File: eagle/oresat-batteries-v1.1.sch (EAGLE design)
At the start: 69 parts, among them IC1 74AHC1G08DBV, U1 TCAN330, U2 STM32F042K6, U3 LTC4411, U4 LTC4411, U5 LTC4411, U6 LTC4411, U7 LTC4412, U8 LTC4412, X1 16MHz

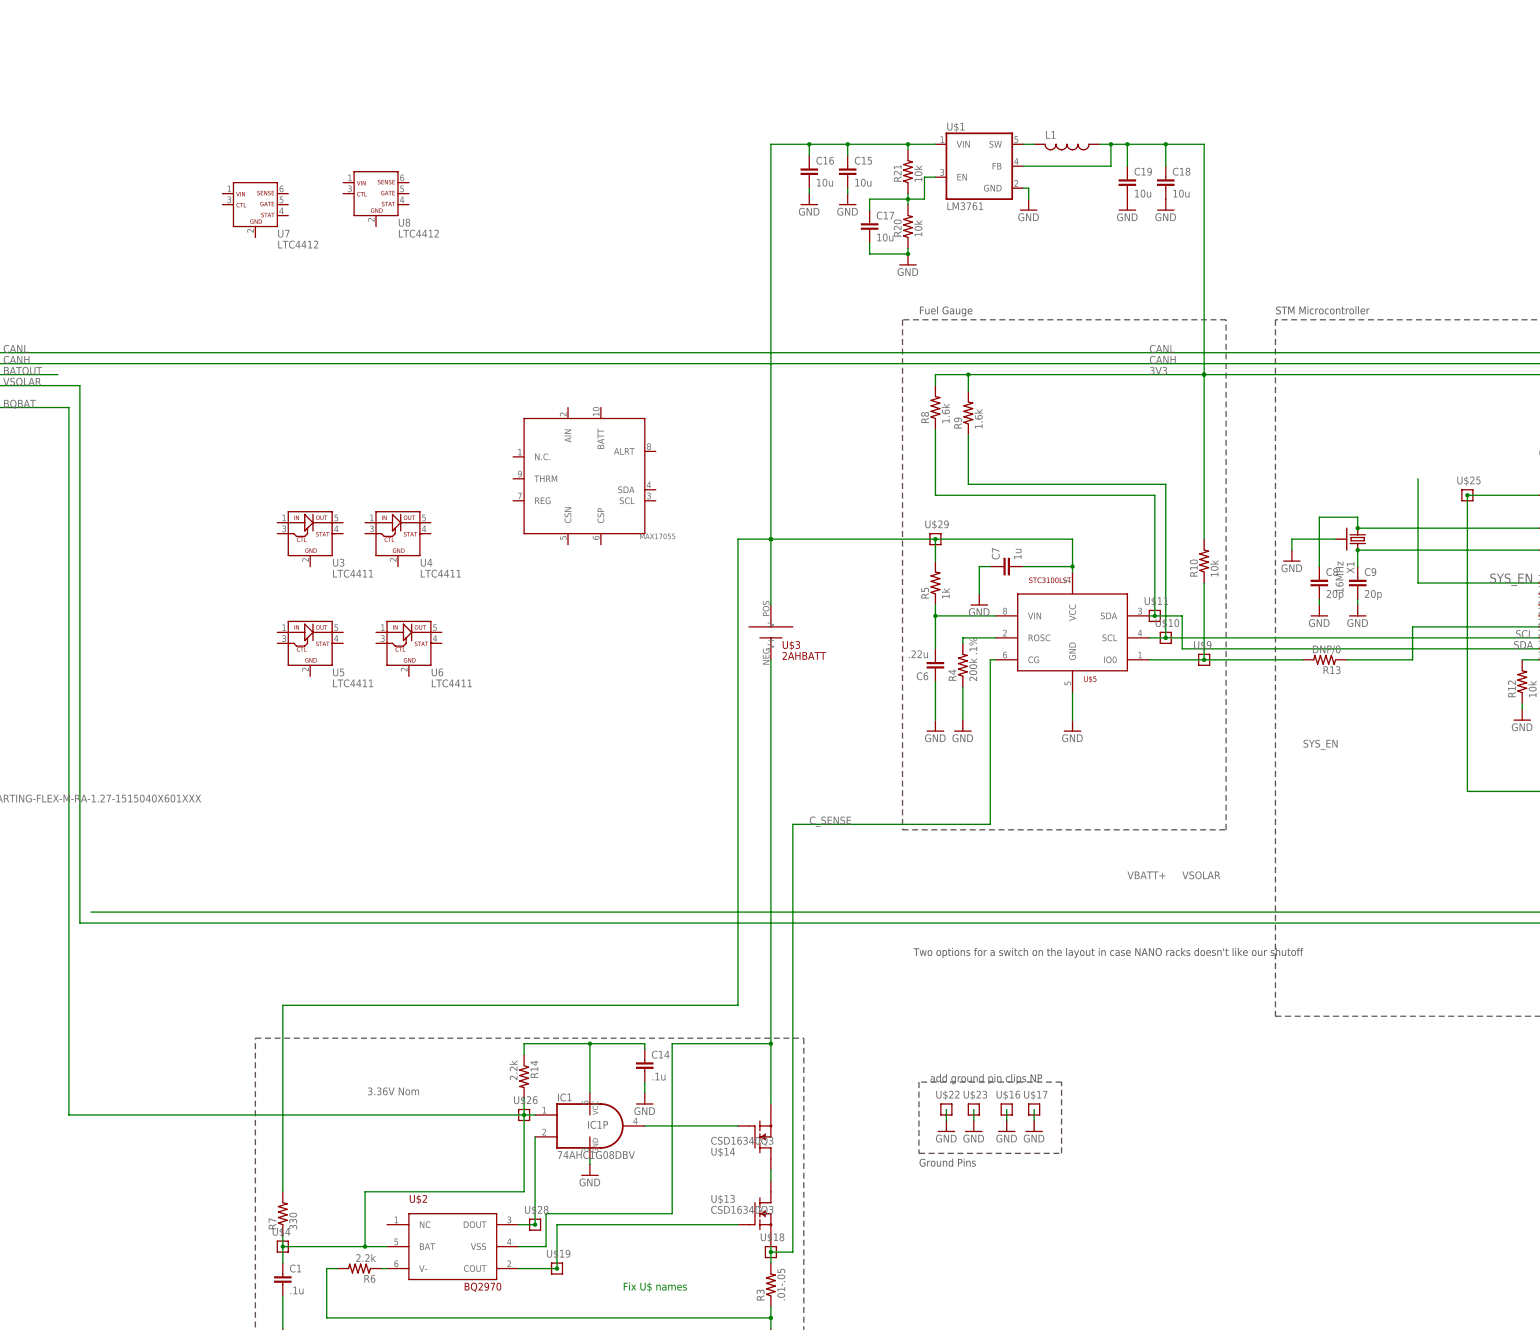
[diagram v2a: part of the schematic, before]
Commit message: Added 4412 and toshiba P-Channel Mosfets.
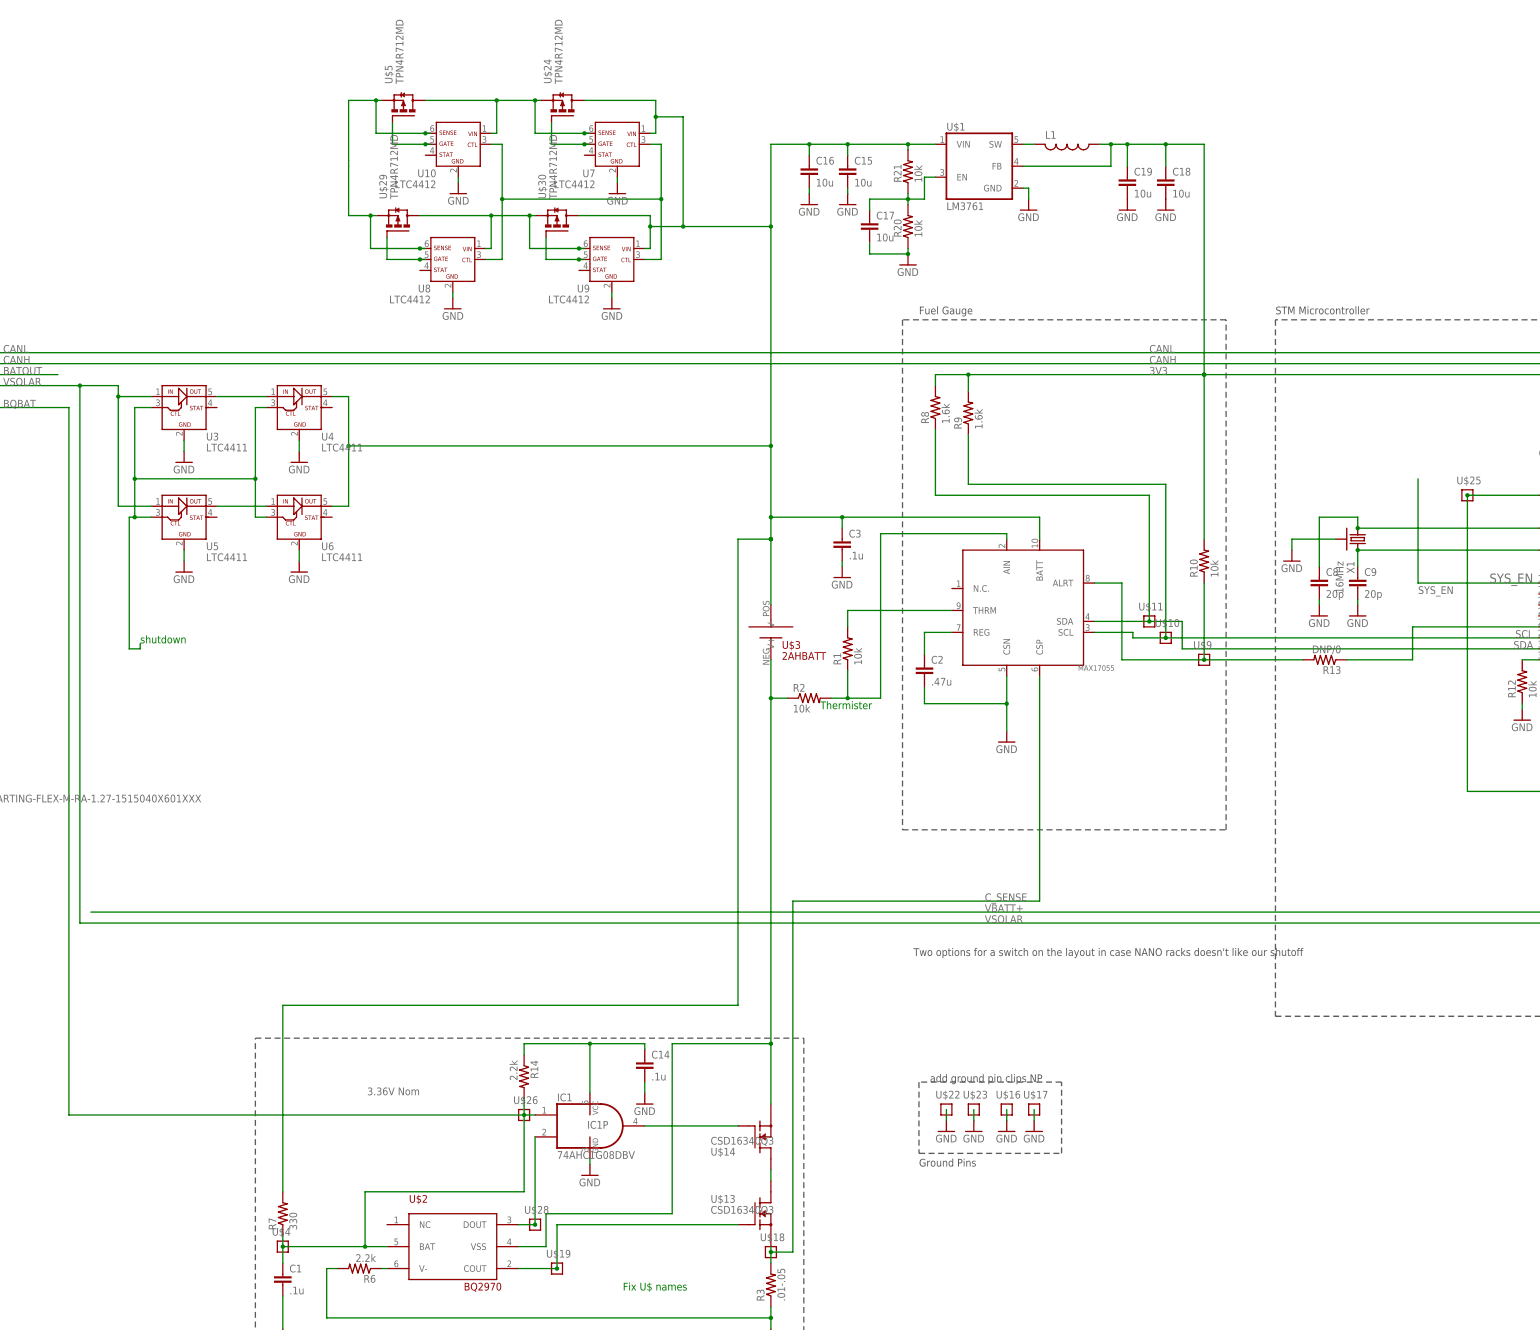
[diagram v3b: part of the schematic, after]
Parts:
- removed C6: .22u, rcl:C-EUC0603
- removed C7: 1u, rcl:C-EUC0805
- removed R4: 200k .1%, rcl:R-US_R0603
- removed R5: 1k, rcl:R-US_R0603
- added C2: .47u, rcl:C-EUC0603
- added C3: .1u, rcl:C-EUC0603
- added R1, R2: 10k, rcl:R-US_R0603
- added U$24, U$30: TPN4R712MD, tpn4r712md-pmosfet:TPN4R712MD
- added U10, U9: LTC4412, ltc4412:LTC4412
- U$29: value TP -> TPN4R712MD; device oresat-batteries:TP -> tpn4r712md-pmosfet:TPN4R712MD
- U$5: value STC3100LST -> TPN4R712MD; device oresat-batteries:STC3100LST -> tpn4r712md-pmosfet:TPN4R712MD
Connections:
- removed net IO0: R10.1, R13.2, U$5.IO0, U$9.P$1
- removed net ROSC: R4.2, U$5.ROSC
- removed net STC_CG: U$14.S, U$2.VSS, U$3.V-
- removed net STC_VIN: C6.2, R5.1, U$5.VIN
- new net 4411MB: U5.OUT, U6.IN
- new net 4411_MT: U3.OUT, U4.IN
- new net ALERT: R10.1, R13.2, U$6.ALRT, U$9.P$1
- new net BATT+: C15.1, C16.1, C3.1, R21.2, R7.2, U$1.VIN, U$24.D, U$3.V+, U$30.D, U$6.BATT, U4.OUT, U6.OUT, U7.VIN, U9.VIN
- new net BATT-: R2.1, U$14.S, U$2.VSS, U$3.V-
- new net CHG_SHD: U3.CTL, U4.CTL, U5.CTL, U6.CTL
- new net DSCHG_SHD: U10.CTL, U7.CTL, U8.CTL, U9.CTL
- new net N$11: U$24.S, U$5.D, U10.VIN, U7.SENSE
- new net N$12: U$24.G, U7.GATE
- new net N$16: U$29.G, U8.GATE
- new net N$18: U$29.D, U$30.S, U8.VIN, U9.SENSE
- new net N$19: U$30.G, U9.GATE
- new net N$8: U$5.G, U10.GATE
- new net REG: C2.1, U$6.REG
- new net THRM: R1.2, U$6.THRM
- new net VBATT: U$29.S, U$5.S, U10.SENSE, U8.SENSE
- net C_SENSE: now also U$6.CSP; no longer U$5.CG
- net GND: now also C2.2, C3.2, U$6.CSN, U10.GND, U3.GND, U4.GND, U5.GND, U6.GND, U7.GND, U8.GND, U9.GND; no longer C6.1, C7.1, R4.1, U$5.GND
- net N$3: now also R1.1, R2.2, U$6.AIN; no longer C15.1, C16.1, C7.2, R21.2, R5.2, R7.2, U$1.VIN, U$29.P$1, U$3.V+, U$5.VCC
- net SCL: now also U$6.SCL; no longer U$5.SCL
- net SDA: now also U$6.SDA; no longer U$5.SDA
- net VSOLAR: now also U3.IN, U5.IN
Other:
- note added: "Thermister"
- note added: "shutdown"
- moved on the sheet: U$11, U3, U4, U5, U6, U7, U8

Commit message: Added charge and discharge control, lowside shutdown, test points and finished rough v1.1 design.
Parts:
- added R11, R15, R16, R17, R18, R23, R4, R5: 470k, rcl:R-US_R0603
- added R19, R22: 10k, rcl:R-US_R0603
- added U$31: MC74HC1G04DFT1GOSCT, MC74HC1G04DFT1GOSCT:MC74HC1G04DFT1GOSCT
- added U$32, U$33, U$34, U$35, U$36, U$37, U$38, U$39, U$40, U$41, U$42, U$43, U$44, U$45, U$46, U$47, U$48, U$49, U$50: TP, oresat-batteries:TP
- U$27: value TP -> MC74HC1G04DFT1GOSCT; device oresat-batteries:TP -> MC74HC1G04DFT1GOSCT:MC74HC1G04DFT1GOSCT
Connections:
- removed net BATOUT: CF1.3
- removed net BQBAT: C1.1, CF1.6, IC1A.I0, R14.2, R7.1, U$2.BAT, U$26.P$1, U$4.P$1
- removed net PA8: U$27.P$1, U2.PA8
- removed net SYS_EN: U2.PB0
- removed net VBATT: U$29.S, U$5.S, U10.SENSE, U8.SENSE
- removed net VBATT+: CF2.2
- new net CHG_CTL: CF1.7, R22.1, U$27.INA
- new net DCHG_CTL: CF1.9, R19.1, U$31.INA
- new net LOWSHD: C1.1, CF1.11, IC1A.I0, R14.2, R7.1, U$2.BAT, U$26.P$1, U$4.P$1
- new net U10STAT: R5.2, U10.STAT, U2.PB3
- new net U3STAT: R23.2, U2.PA8, U3.STAT
- new net U4STAT: R17.2, U2.PA6, U4.STAT
- new net U5STAT: R18.2, U2.PA7, U5.STAT
- new net U6STAT: R16.2, U2.PA5, U6.STAT
- new net U7STAT: R15.2, U2.PA4, U7.STAT
- new net U8STAT: R4.2, U2.PB4, U8.STAT
- new net U9STAT: R11.2, U2.PB1, U9.STAT
- net 3V3: now also CF2.2, R11.1, R15.1, R16.1, R17.1, R18.1, R23.1, R4.1, R5.1, U$38.P$1, U$39.P$1
- net BATT+: now also R19.2, R22.2, U$27.VCC, U$31.VCC, U$50.P$1
- net CANH: now also U$42.P$1
- net CANL: now also U$43.P$1
- net CHG_SHD: now also U$27.OUT, U$47.P$1, U$48.P$1
- net DSCHG_SHD: now also U$31.OUT, U$46.P$1
- net GND: now also U$27.GND, U$31.GND
- net NRESET: now also U$37.P$1
- net SCL: now also R8.1; no longer R9.1
- net SDA: now also R9.1; no longer R8.1
- net STM_DEBUG: now also U$32.P$1
- net SWCLK: now also U$36.P$1
- net SWDIO: now also U$35.P$1
- net USART2_RX: now also U$33.P$1, U$41.P$1, U$44.P$1
- net USART2_TX: now also U$34.P$1, U$40.P$1
- net VSOLAR: now also CF1.3, CF1.5, CF1.6, DEBUG_DNP.10, DEBUG_DNP.9, U$29.S, U$45.P$1, U$49.P$1, U$5.S, U10.SENSE, U8.SENSE
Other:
- note added: "- Do we need an inverter per ctl on the 441x chips? - Do we need the status of the 441X chips and should we control CHG and DCHG with the MCU? - Do we care about MAX alert pin? - Still need to select a thermister. - Still need to select fuses. - Look at heater. - What do you think of these P-FETs? - Recalculate i2c pull-ups. - Change test points from U$ to TP*"
- note removed: "SYS_EN"
- note removed: "Two options for a switch on the layout in case NANO racks doesn't like our shutoff"
- note removed: "VBATT+"
- note removed: "add ground pin clips NP"
- note removed: "shutdown"
- moved on the sheet: C1, C10, C11, C12, C13, C14, C15, C16, C17, C18, C19, C2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

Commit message: Added double pin header.
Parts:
- removed R11, R15, R18, R23: 470k, rcl:R-US_R0603
- added JP2: (no value), pinhead:PINHD-2X20
- R8, R9: value 1.6k -> 4.7k
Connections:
- removed net LOWSHD: C1.1, CF1.11, IC1A.I0, R14.2, R7.1, U$2.BAT, U$26.P$1, U$4.P$1
- removed net N$6: C14.1, IC1P.VCC, R14.1
- removed net U10STAT: R5.2, U10.STAT, U2.PB3
- removed net U4STAT: R17.2, U2.PA6, U4.STAT
- removed net U5STAT: R18.2, U2.PA7, U5.STAT
- removed net U8STAT: R4.2, U2.PB4, U8.STAT
- new net N$4: U2.PA8
- new net SPARE1: CF1.19, CF1.20, JP2.19
- new net SPARE10: CF1.37, CF1.38, JP2.37
- new net SPARE11: CF1.39, CF1.40, JP2.39
- new net SPARE2: CF1.21, CF1.22, JP2.21
- new net SPARE3: CF1.23, CF1.24, JP2.23
- new net SPARE4: CF1.25, CF1.26, JP2.25
- new net SPARE5: CF1.27, CF1.28, JP2.27
- new net SPARE6: CF1.29, CF1.30, JP2.29
- new net SPARE7: CF1.31, CF1.32, JP2.31
- new net SPARE8: CF1.33, CF1.34, JP2.33
- new net SPARE9: CF1.35, CF1.36, JP2.35
- new net SYSSHD: C1.1, CF1.17, CF1.18, IC1A.I0, JP2.17, JP2.18, R14.2, R7.1, U$2.BAT, U$26.P$1, U$4.P$1
- net 3V3: no longer R11.1, R15.1, R18.1, R23.1
- net BATT+: now also C14.1, IC1P.VCC, R14.1
- net BATT-: no longer R2.1
- net CANH: now also CF1.3, CF1.4, JP2.3, JP2.4; no longer CF1.2
- net CANL: now also CF1.2, JP2.1, JP2.2
- net CHG_CTL: now also CF1.13, CF1.14, JP2.13, JP2.14; no longer CF1.7
- net C_SENSE: now also R2.1, R6.2
- net DCHG_CTL: now also CF1.15, CF1.16, JP2.15, JP2.16; no longer CF1.9
- net GND: now also CF1.11, CF1.12, CF1.5, CF1.6, JP2.11, JP2.5; no longer R6.2
- net U3STAT: now also R17.2, U2.PA6, U4.STAT; no longer R23.2, U2.PA8
- net U6STAT: now also U5.STAT
- net U7STAT: now also R5.2, U10.STAT, U2.PB3; no longer R15.2, U2.PA4
- net U9STAT: now also R4.2, U2.PB4, U8.STAT; no longer R11.2, U2.PB1
- net VSOLAR: now also CF1.10, CF1.7, CF1.8, CF1.9, JP2.6, JP2.7, JP2.8, JP2.9; no longer CF1.3, CF1.4, CF1.5, CF1.6
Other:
- moved on the sheet: CF1

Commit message: Fixed most of the issues from design review Sept 25.
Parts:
- removed C16, C17, C18, C19: 10u, rcl:C-EUC0805
- removed DEBUG_DNP: (no value), pinhead:PINHD-2X8
- removed R21, R22: 10k, rcl:R-US_R0603
- removed U$1: LM3761, oresat-batteries:LM3761
- removed U$13, U$14: CSD16340Q3, oresat-batteries:CSD16340Q3
- removed U$16, U$17, U$18, U$19, U$22, U$23, U$26, U$28, U$4, U$41, U$44, U$46, U$47, U$48, U$49, U$50: TP, oresat-batteries:TP
- removed U$2: BQ2970, oresat-batteries:BQ2970
- removed U$21: 4.19, oresat-batteries:RES_HEATER
- removed U$24, U$29, U$30, U$5: TPN4R712MD, tpn4r712md-pmosfet:TPN4R712MD
- removed U$27, U$31: MC74HC1G04DFT1GOSCT, MC74HC1G04DFT1GOSCT:MC74HC1G04DFT1GOSCT
- removed U$3: 2AHBATT, oresat-batteries:2AHBATT
- removed U$6: MAX17055, max17055:MAX17055
- added B1: 2AHBATT, oresat-batteries:2AHBATT
- added C4, C7: .1u, rcl:C-EUC0603
- added C5, C6: 10u, rcl:C-EUC0805
- added D1, D2, D3: CMDD6001, CMMDD6001:CMDD6001
- added JP1: (no value), pinhead:PINHD-2X20
- added Q1, Q2: CSD16340Q3, oresat-batteries:CSD16340Q3
- added Q3, Q4, Q5, Q6: TPN4R712MD, tpn4r712md-pmosfet:TPN4R712MD
- added R11: 4.7k, rcl:R-US_R0603
- added R15, R18: 470k, rcl:R-US_R0603
- added TP1, TP10, TP11, TP12, TP13, TP14, TP19, TP2, TP20, TP3, TP4, TP5, TP6, TP7, TP8, TP9: TP, oresat-batteries:TP
- added U11: MAX17055, max17055:MAX17055
- added U12, U13: LTC4412, ltc4412:LTC4412
- added U14: STM32F042K6, oresat-batteries:STM32F042K6
- added U15: TCAN330, oresat-batteries:TCAN330
- C1, C3: value .1u -> 10u; device rcl:C-EUC0603 -> rcl:C-EUC0805
- C10, C11: value 100n -> 20p
- C14: value .1u -> 100n
- C15: value 10u -> 100n; device rcl:C-EUC0805 -> rcl:C-EUC0603
- C2: value .47u -> 10u; device rcl:C-EUC0603 -> rcl:C-EUC0805
- C8: value 20p -> .1u
- C9: value 20p -> .47u
- JP2: device pinhead:PINHD-2X20 -> pinhead:PINHD-2X8
- R1: value 10k -> 330
- R12: value 10k -> 4.7k
- R13: value DNP/0 -> 10k
- R14: value 2.2k -> 470k
- R16: value 470k -> DNP/0
- R20: value 10k -> 4.19; device rcl:R-US_R0603 -> oresat-batteries:RES_HEATER
- R3: value .01-.05 -> 10k
- R4: value 470k -> 10k
- R5: value 470k -> 2.2k
- R7: value 330 -> .01-.05
- R8, R9: value 4.7k -> 10k
- U1: value TCAN330 -> LM3761; device oresat-batteries:TCAN330 -> oresat-batteries:LM3761
- U2: value STM32F042K6 -> MC74HC1G04DFT1GOSCT; device oresat-batteries:STM32F042K6 -> MC74HC1G04DFT1GOSCT:MC74HC1G04DFT1GOSCT
- U3: value LTC4411 -> BQ2970; device ltc4411:LTC4411 -> oresat-batteries:BQ2970
- U7: value LTC4412 -> LTC4411; device ltc4412:LTC4412 -> ltc4411:LTC4411
- U8: value LTC4412 -> MC74HC1G04DFT1GOSCT; device ltc4412:LTC4412 -> MC74HC1G04DFT1GOSCT:MC74HC1G04DFT1GOSCT
- renumbered CF1 to CM1, CF2 to J1, U$10 to TP15, U$11 to TP16, U$12 to TP31, U$15 to TP30, U$20 to Q7, U$25 to TP18, U$32 to TP23, U$33 to TP24, U$34 to TP25, U$35 to TP26, U$36 to TP27, U$37 to TP28, U$38 to TP29, U$39 to TP22, U$40 to TP21, U$42 to TP34, U$43 to TP33, U$45 to TP35, U$8 to TP32, U$9 to TP17
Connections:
- removed net 3V3: C10.1, C11.1, C12.1, C13.1, C18.1, C19.1, DEBUG_DNP.1, DEBUG_DNP.2, J1.2, L1.1, Q7.D, R10.2, R16.1, R17.1, R4.1, R5.1, R8.2, R9.2, TP22.P$1, TP29.P$1, TP30.P$1, U$1.FB, U1.VCC, U2.VDD, U2.VDDA, U2.VDDIO2
- removed net BATT+: C14.1, C15.1, C16.1, C3.1, IC1P.VCC, R14.1, R19.2, R21.2, R22.2, R7.2, U$1.VIN, U$24.D, U$27.VCC, U$3.V+, U$30.D, U$31.VCC, U$50.P$1, U$6.BATT, U4.OUT, U6.OUT, U7.VIN, U9.VIN
- new net 3.3V: C12.1, C13.1, C14.1, C15.1, C5.1, C6.1, J1.2, JP2.1, JP2.2, L1.1, Q7.D, R11.2, R12.2, R13.2, R14.1, R15.1, R17.1, R18.1, TP22.P$1, TP29.P$1, TP30.P$1, U1.FB, U14.VDD, U14.VDDA, U14.VDDIO2, U15.VCC
- new net N$10: D3.A, R4.1, U2.INA
- new net N$6: D1.C, JP1.18
- new net N$9: D2.C, JP1.16
- new net VBATT: B1.V+, C1.1, C2.1, C7.1, C8.1, IC1P.VCC, Q3.D, Q4.D, R1.2, R2.2, R4.2, R6.1, R8.2, TP12.P$1, U1.VIN, U10.VIN, U11.BATT, U2.VCC, U6.OUT, U7.OUT, U8.VCC, U9.VIN
- net 4411MB: now also U7.IN; no longer U6.IN
- net 4411_MT: now also U4.OUT, U6.IN; no longer U3.OUT, U4.IN
- net ALERT: now also R13.1, R16.2, U11.ALRT; no longer R10.1, R13.2, U$6.ALRT
- net ANDDRIVE: now also Q1.G; no longer U$14.G
- net BATT-: now also B1.V-, Q1.S, U3.VSS; no longer U$14.S, U$2.VSS, U$3.V-
- net BETSHUT: now also Q1.D, Q2.D; no longer U$13.D, U$14.D
- net BQVMIN: now also R5.1, U3.V-; no longer R6.1, U$2.V-
- net CANH: now also JP1.3, JP1.4, JP2.13, JP2.14, U15.CANH; no longer DEBUG_DNP.13, DEBUG_DNP.14, JP2.3, JP2.4, U1.CANH
- net CANL: now also JP1.1, JP1.2, JP2.11, JP2.12, U15.CANL; no longer DEBUG_DNP.11, DEBUG_DNP.12, JP2.1, JP2.2, U1.CANL
- net CAN_EN: now also U14.PA10, U15.SHDN; no longer U1.SHDN, U2.PA10
- net CAN_LSTN: now also U14.PA9, U15.S; no longer U1.S, U2.PA9
- net CAN_RX: now also U14.PA11, U15.RXD; no longer U1.RXD, U2.PA11
- net CAN_TX: now also U14.PA12, U15.TXD; no longer U1.TXD, U2.PA12
- net CHG_CTL: now also D3.C, JP1.13, JP1.14; no longer JP2.13, JP2.14, R22.1, U$27.INA
- net CHG_SHD: now also TP10.P$1, TP11.P$1, U2.OUT, U7.CTL; no longer U$27.OUT, U$47.P$1, U$48.P$1, U3.CTL
- net COUT: now also Q2.G, TP9.P$1, U3.COUT; no longer U$13.G, U$19.P$1, U$2.COUT
- net C_SENSE: now also Q2.S, R5.2, R7.2, R9.1, TP13.P$1, U11.CSP; no longer R2.1, R3.2, R6.2, U$13.S, U$18.P$1, U$6.CSP
- net DCHG_CTL: now also D2.A, JP1.15, R8.1, U8.INA; no longer JP2.15, JP2.16, R19.1, U$31.INA
- net DSCHG_SHD: now also TP14.P$1, U12.CTL, U13.CTL, U8.OUT; no longer U$31.OUT, U$46.P$1, U7.CTL, U8.CTL
- net GND: now also C4.2, C5.2, C6.2, C7.2, JP1.11, JP1.5, JP2.15, JP2.16, R19.1, R20.2, R7.1, TP1.P$1, TP2.P$1, TP3.P$1, TP4.P$1, U11.CSN, U12.GND, U13.GND, U14.VSS, U15.GND, U2.GND; no longer C16.2, C17.2, C18.2, C19.2, DEBUG_DNP.15, DEBUG_DNP.16, JP2.11, JP2.5, R12.1, R20.1, U$1.GND, U$16.P$1, U$17.P$1, U$21.2, U$22.P$1, U$23.P$1, U$27.GND, U$31.GND, U$6.CSN, U2.VSS, U3.GND
- net HEAT: now also U14.PA1; no longer U2.PA1
- net N$1: now also U1.SW; no longer U$1.SW
- net N$11: now also Q3.S, Q5.D, U12.VIN, U9.SENSE; no longer U$24.S, U$5.D, U10.VIN, U7.SENSE
- net N$12: now also Q3.G, U9.GATE; no longer U$24.G, U7.GATE
- net N$13: now also R20.1; no longer U$21.1
- net N$16: now also Q6.G, U13.GATE; no longer U$29.G, U8.GATE
- net N$18: now also Q4.S, Q6.D, U10.SENSE, U13.VIN; no longer U$29.D, U$30.S, U8.VIN, U9.SENSE
- net N$19: now also Q4.G, U10.GATE; no longer U$30.G, U9.GATE
- net N$2: now also R19.2, U14.PB8-BOOT0; no longer R12.2, U2.PB8-BOOT0
- net N$3: now also R10.1, R9.2, U11.AIN; no longer R1.1, R2.2, U$6.AIN
- net N$4: now also U14.PA8; no longer U2.PA8
- net N$5: now also TP8.P$1, U3.DOUT; no longer U$2.DOUT, U$28.P$1
- net N$7: now also C3.1, R2.1, R3.2, U1.EN; no longer C17.1, R20.2, R21.1, U$1.EN
- net N$8: now also Q5.G, U12.GATE; no longer U$5.G, U10.GATE
- net NRESET: now also U14.NRST; no longer U2.NRST
- net OSC_IN: now also C10.1, U14.PF0-OSC_IN; no longer C8.1, U2.PF0-OSC_IN
- net OSC_OUT: now also C11.1, U14.PF1-OSC_OUT; no longer C9.1, U2.PF1-OSC_OUT
- net REG: now also C9.1, U11.REG; no longer C2.1, U$6.REG
- net SCL: now also R11.1, U11.SCL, U14.PB6; no longer R8.1, U$6.SCL, U2.PB6
- net SDA: now also R12.1, U11.SDA, U14.PB7; no longer R9.1, U$6.SDA, U2.PB7
- net SPARE1: now also JP1.19; no longer JP2.19
- net SPARE10: now also JP1.37; no longer JP2.37
- net SPARE11: now also JP1.39; no longer JP2.39
- net SPARE2: now also JP1.21; no longer JP2.21
- net SPARE3: now also JP1.23; no longer JP2.23
- net SPARE4: now also JP1.25; no longer JP2.25
- net SPARE5: now also JP1.27; no longer JP2.27
- net SPARE6: now also JP1.29; no longer JP2.29
- net SPARE7: now also JP1.31; no longer JP2.31
- net SPARE8: now also JP1.33; no longer JP2.33
- net SPARE9: now also JP1.35; no longer JP2.35
- net STC_IO: now also R16.1, U14.PB5; no longer R13.1, U2.PB5
- net STM_DEBUG: now also U14.PA0; no longer U2.PA0
- net SWCLK: now also U14.PA14-SWCLK; no longer U2.PA14-SWCLK
- net SWDIO: now also U14.PA13-SWDIO; no longer U2.PA13-SWDIO
- net SYSSHD: now also C4.1, D1.A, JP1.17, R1.1, R6.2, TP5.P$1, TP7.P$1, U3.BAT; no longer C1.1, JP2.17, JP2.18, R14.2, R7.1, U$2.BAT, U$26.P$1, U$4.P$1
- net THRM: now also R10.2, U11.THRM; no longer R1.2, U$6.THRM
- net U3STAT: now also R18.2, U14.PA6, U6.STAT; no longer R17.2, U2.PA6, U3.STAT
- net U6STAT: now also R17.2, U14.PA5, U7.STAT; no longer R16.2, U2.PA5, U6.STAT
- net U7STAT: now also R15.2, U12.STAT, U14.PB3, U9.STAT; no longer R5.2, U10.STAT, U2.PB3, U7.STAT
- net U9STAT: now also R14.2, U10.STAT, U13.STAT, U14.PB4; no longer R4.2, U2.PB4, U8.STAT, U9.STAT
- net USART2_RX: now also JP2.5, JP2.6, TP19.P$1, TP20.P$1, U14.PA3; no longer DEBUG_DNP.5, DEBUG_DNP.6, U$41.P$1, U$44.P$1, U2.PA3
- net USART2_TX: now also JP2.3, JP2.4, U14.PA2; no longer DEBUG_DNP.3, DEBUG_DNP.4, U2.PA2
- net VSOLAR: now also JP1.6, JP1.7, JP1.8, JP1.9, JP2.10, Q5.S, Q6.S, TP6.P$1, U12.SENSE, U13.SENSE, U4.IN; no longer DEBUG_DNP.10, DEBUG_DNP.7, DEBUG_DNP.8, DEBUG_DNP.9, JP2.6, U$29.S, U$49.P$1, U$5.S, U10.SENSE, U3.IN, U8.SENSE
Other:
- note added: "- Still need to select a thermister. - Still need to select fuses. - Still need diodes and connection to MCU from CHG/DCHG_CTL - Change test points from U$ to TP* - Change mostfets to Q$"
- note removed: "- Do we need an inverter per ctl on the 441x chips? - Do we need the status of the 441X chips and should we control CHG and DCHG with the MCU? - Do we care about MAX alert pin? - Still need to select a thermister. - Still need to select fuses. - Look at heater. - What do you think of these P-FETs? - Recalculate i2c pull-ups. - Change test points from U$ to TP*"
- moved on the sheet: C1, C10, C11, C13, C14, C15, C2, C3, C8, C9, IC1, IC1P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

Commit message: Cosmetics.
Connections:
- new net 5V: C8.1, U11.BATT
- net VBATT: no longer C8.1, U11.BATT
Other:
- moved on the sheet: C8, R15, R17, R18, TP33, TP34

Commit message: Cosmetics again.
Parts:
- removed TP10: TP, oresat-batteries:TP
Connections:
- net STC_IO renamed MAX_IO
- removed net N$10: D3.A, R4.1, U2.INA
- removed net N$9: D2.C, JP1.16
- new net !SHUTDOWN: CM1.7, CM1.8, JP1.7
- new net TO_CHG: D3.A, R4.1, U14.PB3, U2.INA
- new net TO_DCHG: D2.A, R8.1, U14.PB4, U8.INA
- net BATT-: now also TP20.P$1
- net CHG_CTL: now also CM1.15, CM1.16, JP1.15, JP1.16; no longer CM1.13, CM1.14, JP1.13, JP1.14
- net CHG_SHD: no longer TP10.P$1
- net DCHG_CTL: now also CM1.17, CM1.18, D2.C, JP1.17, JP1.18; no longer CM1.15, CM1.16, D2.A, JP1.15, R8.1, U8.INA
- net GND: now also CM1.10, CM1.9, JP1.10, JP1.6, JP1.9; no longer CM1.11, CM1.12, JP1.11
- net N$16: now also U13.SENSE
- net N$6: now also JP1.8; no longer JP1.18
- net SYSSHD: no longer CM1.17, CM1.18, JP1.17
- net U7STAT: now also U14.PB0; no longer U14.PB3
- net U9STAT: now also U14.PB1; no longer U14.PB4
- net USART2_RX: no longer TP20.P$1
- net VSOLAR: now also CM1.11, CM1.12, CM1.13, CM1.14, JP1.11, JP1.12, JP1.13, JP1.14; no longer CM1.10, CM1.7, CM1.8, CM1.9, JP1.6, JP1.7, JP1.8, JP1.9, U13.SENSE
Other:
- moved on the sheet: C4, D1, D2, D3, R1, R4, R8, TP20, TP5, TP6, U2, U8
